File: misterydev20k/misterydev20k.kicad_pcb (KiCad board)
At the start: 2 copper layers, 90 x 67 mm, 188 parts, among them J1 SWD, J11 Joystick 0, J12 Joystick 1, J13 USB_A_Stacked, J2 USB_C_Receptacle_USB2.0, J3 Jumper block, J4 Micro_SD_Card_Det1, J5 HDMI_A, J6 Grove 1125S-4P, J7 USB_A_Stacked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

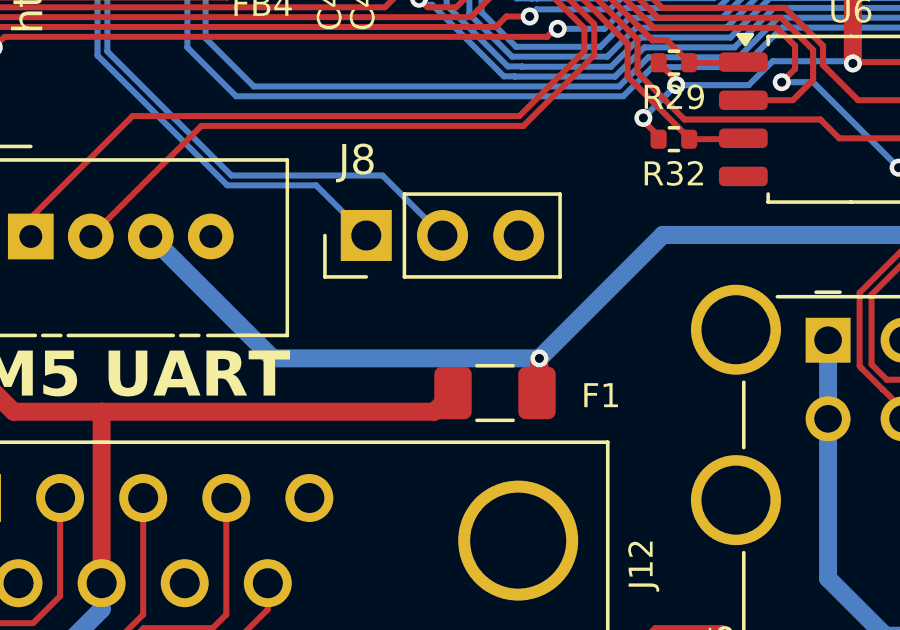
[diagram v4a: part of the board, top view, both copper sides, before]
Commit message: Fix JLCPCB footprint offset and rotation
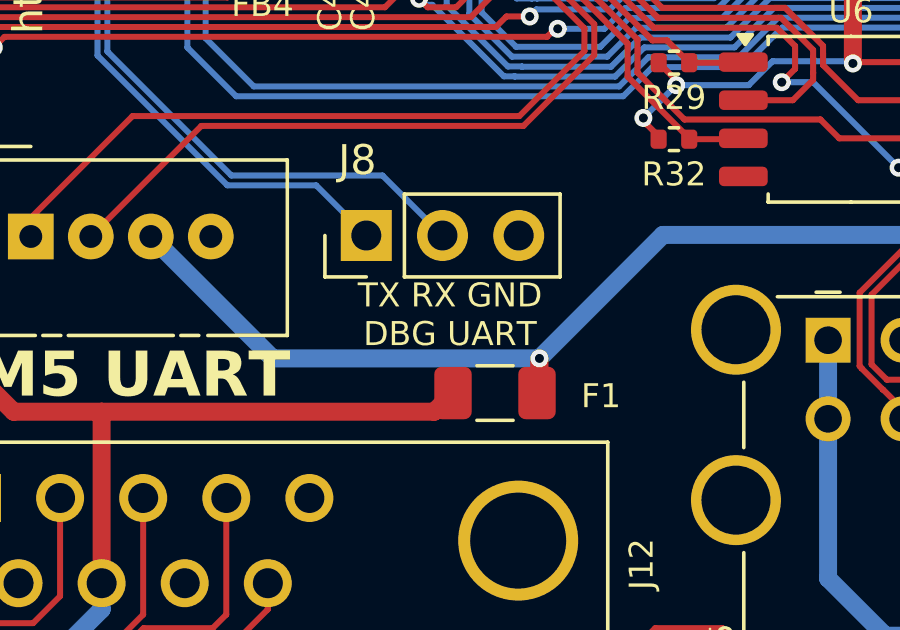
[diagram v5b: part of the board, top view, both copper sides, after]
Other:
- board text added: "TX RX GND DBG UART"
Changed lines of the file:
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@@
 		(sheetname "/GW2AR-LV18 FPGA/Interfaces/")
 		(sheetfile "interfaces.kicad_sch")
-		(attr through_hole)
+		(attr through_hole exclude_from_bom)
 		(fp_line
 			(start 3 -3)
@@
 			)
 		)
+		(property "JLCPCB Rotation Offset" "180"
+			(at 0 0 90)
+			(unlocked yes)
+			(layer "F.Fab")
+			(hide yes)
+			(effects
+				(font
+					(size 1 1)
+					(thickness 0.15)
+				)
+			)
+		)
+		(property "FT Rotation Offset" "90"
+			(at 0 0 90)
+			(unlocked yes)
+			(layer "F.Fab")
+			(hide yes)
+			(effects
+				(font
+					(size 1 1)
+					(thickness 0.15)
+				)
+			)
+		)
 		(property ki_fp_filters "SOIC*3.9x8.7mm*P1.27mm* TSSOP*4.4x5mm*P0.65mm* DIP*W7.62mm*")
 		(sheetname "/GW2AR-LV18 FPGA/Interfaces/")
@@
 			)
 		)
+		(property "JLCPCB Rotation Offset" "180"
+			(at 0 0 180)
+			(unlocked yes)
+			(layer "F.Fab")
+			(hide yes)
+			(effects
+				(font
+					(size 1 1)
+					(thickness 0.15)
+				)
+			)
+		)
+		(property "FT Rotation Offset" "90"
+			(at 0 0 180)
+			(unlocked yes)
+			(layer "F.Fab")
+			(hide yes)
+			(effects
+				(font
+					(size 1 1)
+					(thickness 0.15)
+				)
+			)
+		)
 		(property ki_fp_filters "Connector*:*_1x??_*")
 		(sheetname "/")
@@
 			)
 		)
+		(property "FT Rotation Offset" "90"
+			(at 0 0 90)
+			(unlocked yes)
+			(layer "F.Fab")
+			(hide yes)
+			(effects
+				(font
+					(size 1 1)
+					(thickness 0.15)
+				)
+			)
+		)
 		(property ki_fp_filters "SOT?23*")
 		(sheetname "/")
@@
 			)
 		)
-		(property "JLCPCB Rotation Offset" "270"
+		(property "JLCPCB Rotation Offset" "180"
 			(at 0 0 270)
 			(unlocked yes)
@@
 			)
 		)
+		(property "FT Rotation Offset" "270"
+			(at 0 0 270)
+			(unlocked yes)
+			(layer "F.Fab")
+			(hide yes)
+			(effects
+				(font
+					(size 1 1)
+					(thickness 0.15)
+				)
+			)
+		)
+		(property "FT Position Offset" "1,5.5"
+			(at 0 0 270)
+			(unlocked yes)
+			(layer "F.Fab")
+			(hide yes)
+			(effects
+				(font
+					(size 1 1)
+					(thickness 0.15)
+				)
+			)
+		)
 		(property ki_fp_filters "DSUB*Male*")
 		(sheetname "/GW2AR-LV18 FPGA/Interfaces/")
@@
 			)
 		)
+		(property "JLCPCB Rotation Offset" "180"
+			(at 0 0 90)
+			(unlocked yes)
+			(layer "F.Fab")
+			(hide yes)
+			(effects
+				(font
+					(size 1 1)
+					(thickness 0.15)
+				)
+			)
+		)
+		(property "FT Rotation Offset" "90"
+			(at 0 0 90)
+			(unlocked yes)
+			(layer "F.Fab")
+			(hide yes)
+			(effects
+				(font
+					(size 1 1)
+					(thickness 0.15)
+				)
+			)
+		)
 		(property ki_fp_filters "HDMI*A*")
 		(sheetname "/GW2AR-LV18 FPGA/Interfaces/")
@@
 			)
 		)
-		(property "JLCPCB Rotation Offset" "270"
+		(property "JLCPCB Rotation Offset" "180"
 			(at 0 0 0)
 			(unlocked yes)
@@
 			)
 		)
+		(property "FT Rotation Offset" "270"
+			(at 0 0 0)
+			(unlocked yes)
+			(layer "F.Fab")
+			(hide yes)
+			(effects
+				(font
+					(size 1 1)
+					(thickness 0.15)
+				)
+			)
+		)
+		(property "FT Position Offset" "1,5.5"
+			(at 0 0 0)
+			(unlocked yes)
+			(layer "F.Fab")
+			(hide yes)
+			(effects
+				(font
+					(size 1 1)
+					(thickness 0.15)
+				)
+			)
+		)
 		(property ki_fp_filters "DSUB*Male*")
 		(sheetname "/GW2AR-LV18 FPGA/Interfaces/")
@@
 			)
 		)
-		(property "LCSC Part #" "C6837606"
+		(property "LCSC Part #" "C32713279"
+			(at 0 0 0)
+			(unlocked yes)
+			(layer "F.Fab")
+			(hide yes)
+			(effects
+				(font
+					(size 1 1)
+					(thickness 0.15)
+				)
+			)
+		)
+		(property "FT Rotation Offset" "90"
 			(at 0 0 0)
 			(unlocked yes)
@@
 			)
 		)
-		(property "checked" ""
+		(property "checked" "once"
+			(at 0 0 270)
+			(unlocked yes)
+			(layer "F.Fab")
+			(hide yes)
+			(effects
+				(font
+					(size 1 1)
+					(thickness 0.15)
+				)
+			)
+		)
+		(property "LCSC Part #" "C9900028472"
 			(at 0 0 270)
 			(unlocked yes)
@@
 		(sheetname "/GW2AR-LV18 FPGA/Interfaces/")
 		(sheetfile "interfaces.kicad_sch")
-		(attr through_hole)
+		(attr through_hole exclude_from_bom)
 		(fp_line
 			(start -1.38 -1.38)
@@
 			)
 		)
+		(property "JLCPCB Position Offset" "0,-4"
+			(at 0 0 180)
+			(unlocked yes)
+			(layer "F.Fab")
+			(hide yes)
+			(effects
+				(font
+					(size 1 1)
+					(thickness 0.15)
+				)
+			)
+		)
+		(property "FT Position Offset" "0,2"
+			(at 0 0 180)
+			(unlocked yes)
+			(layer "F.Fab")
+			(hide yes)
+			(effects
+				(font
+					(size 1 1)
+					(thickness 0.15)
+				)
+			)
+		)
 		(property ki_fp_filters "USB*C*Receptacle*")
 		(sheetname "/")
@@
 			)
 		)
+		(property "JLCPCB Rotation Offset" "180"
+			(at 0 0 90)
+			(unlocked yes)
+			(layer "F.Fab")
+			(hide yes)
+			(effects
+				(font
+					(size 1 1)
+					(thickness 0.15)
+				)
+			)
+		)
+		(property "FT Rotation Offset" "90"
+			(at 0 0 90)
+			(unlocked yes)
+			(layer "F.Fab")
+			(hide yes)
+			(effects
+				(font
+					(size 1 1)
+					(thickness 0.15)
+				)
+			)
+		)
 		(property ki_fp_filters "SOIC*3.9x8.7mm*P1.27mm* TSSOP*4.4x5mm*P0.65mm* DIP*W7.62mm*")
 		(sheetname "/GW2AR-LV18 FPGA/Interfaces/")
@@
 		)
 	)
+	(gr_text "TX RX GND\nDBG UART"
+		(at 135.5 91.5 0)
+		(layer "F.SilkS")
+		(effects
+			(font
+				(size 0.8 0.8)
+				(thickness 0.1)
+			)
+			(justify bottom)
+		)
+	)

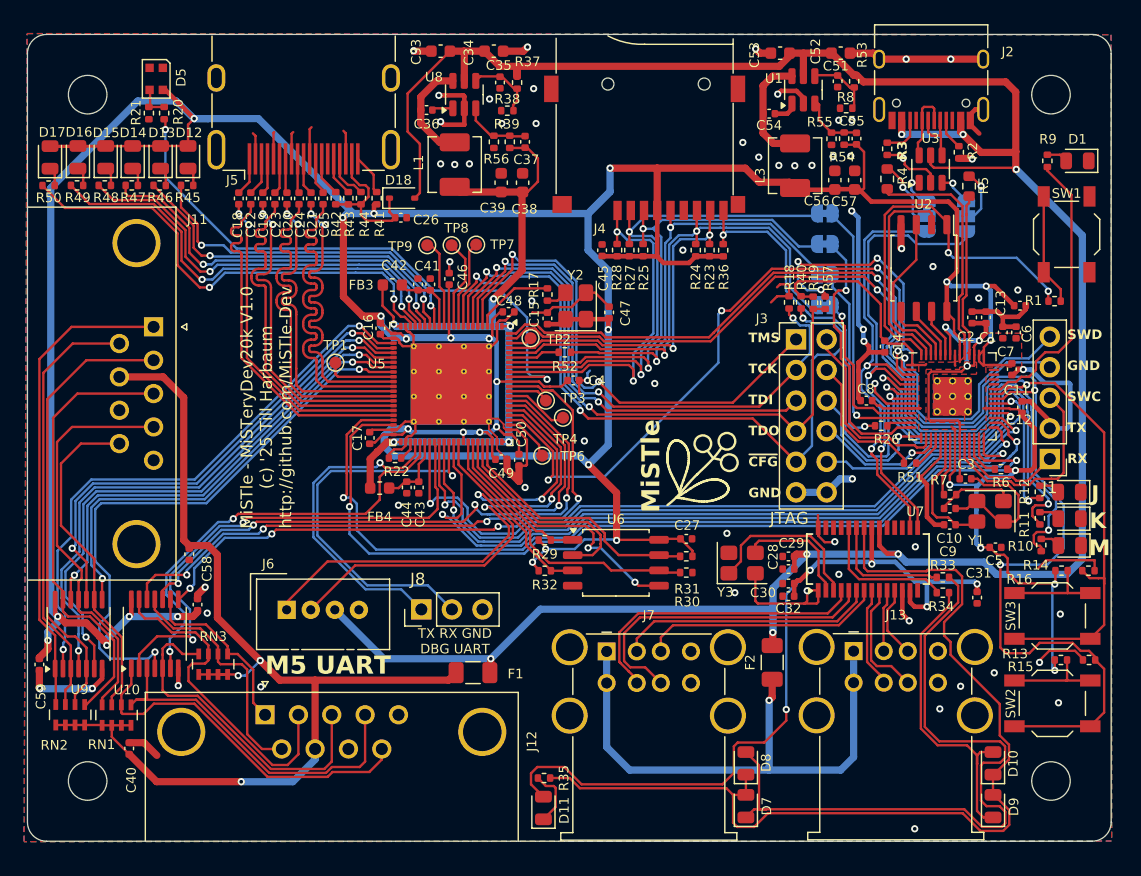
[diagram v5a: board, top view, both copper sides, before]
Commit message: Add hyperram
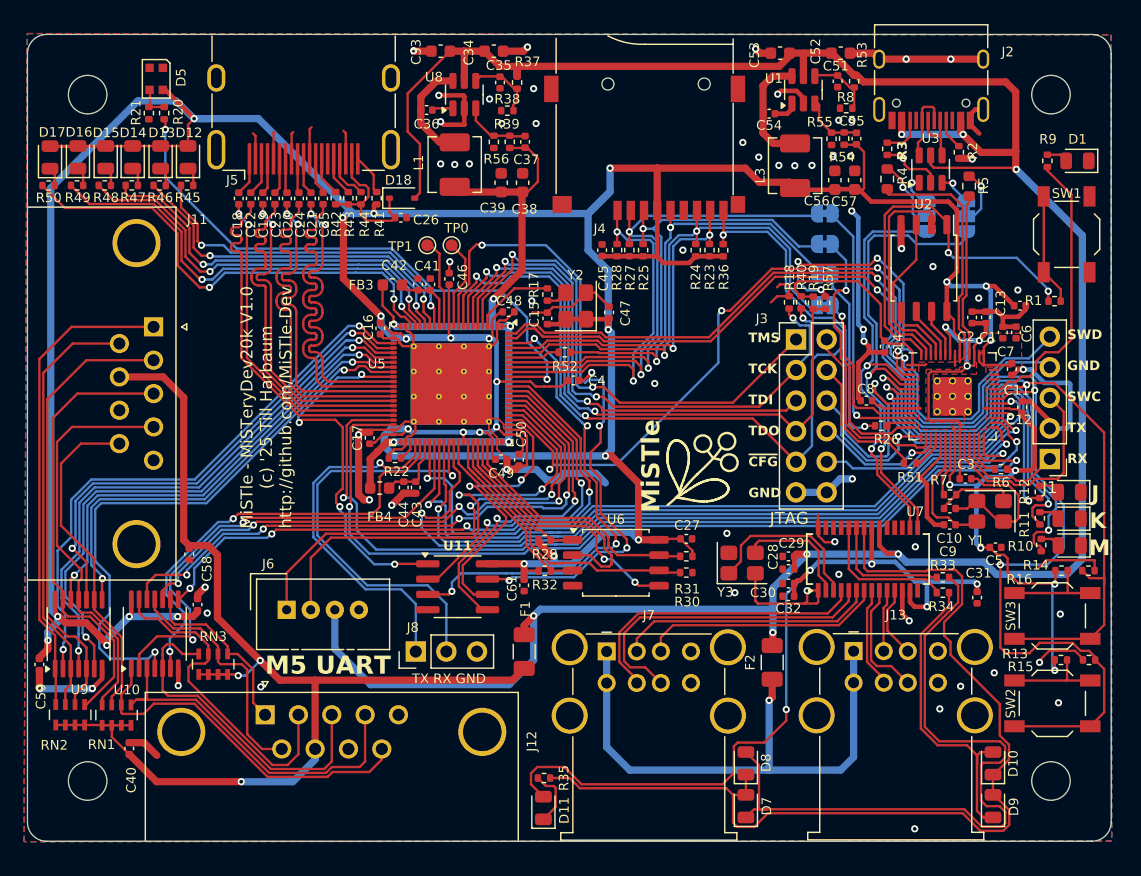
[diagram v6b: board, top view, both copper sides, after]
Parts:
- removed the TP1 at (125.6, 67.3)
- removed TP2, TP3, TP4, TP6, TP7: TestPoint, TestPoint:TestPoint_Pad_D1.0mm
- added C61: 100nF, Capacitor_SMD:C_0402_1005Metric, F.Cu at (141.2, 85.8)
- added U11: LY68L6400SLIT, Package_SO:SOIC-8_3.9x4.9mm_P1.27mm, F.Cu at (135.7, 85.9)
- moved F1 4.60 mm to (141.2, 91.2), turned to 90 degrees
- moved J8 3.53 mm to (132.2, 91.2)
- moved C43 0.25 mm to (132.2, 77.6)
- moved C44 0.25 mm to (131.2, 77.6)
- renumbered TP8 to TP0, TP9 to TP1
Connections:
- U5 pad 10: Net-(U5-IOL29A/GCLKT_6) -> HR_IO3
- U5 pad 32: Net-(U5-IOB18B) -> ~{HR_CS}
- U5 pad 69: Net-(U5-IOT50A) -> HR_CLK
- U5 pad 75: Net-(U5-IOT34A) -> HR_IO0
- U5 pad 76: Net-(U5-IOT30B/GCLKC_1) -> HR_IO1
- U5 pad 86: Net-(U5-IOT4A) -> HR_IO2
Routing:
- net HR_IO3: track 0.00 -> 56.8 mm, vias 0 -> 4
- net HR_IO2: track 0.00 -> 40.3 mm, vias 0 -> 4
- net ~{HR_CS}: track 0.00 -> 31.3 mm, vias 0 -> 4
- net HR_IO0: track 0.00 -> 29.6 mm, vias 0 -> 2
- net HR_IO1: track 0.00 -> 28.9 mm, vias 0 -> 2
- net HR_CLK: track 0.00 -> 24.5 mm, vias 0 -> 2
- net GND: track 253.5 -> 269.9 mm, vias 63 -> 64
- net +3V3: track 437.0 -> 446.1 mm
- net Net-(U5-IOL29A/GCLKT_6): track 7.38 -> 0.00 mm
- net +5V: track 211.9 -> 218.4 mm
- net Net-(U5-IOB18B): track 5.87 -> 0.00 mm
- net Net-(RN1-R1.2): track 88.3 -> 94.1 mm
- net Net-(U5-IOT34A): track 5.39 -> 0.00 mm
- net Net-(U5-IOT50A): track 4.18 -> 0.00 mm
- net Net-(U5-IOT30B/GCLKC_1): track 3.43 -> 0.00 mm
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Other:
- board text added: "TX RX GND"
- board text removed: "TX RX GND DBG UART"
